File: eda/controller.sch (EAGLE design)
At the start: 17 parts, among them U1 STM32F405/7R, Y1 8 MHz/C_L=15 pF

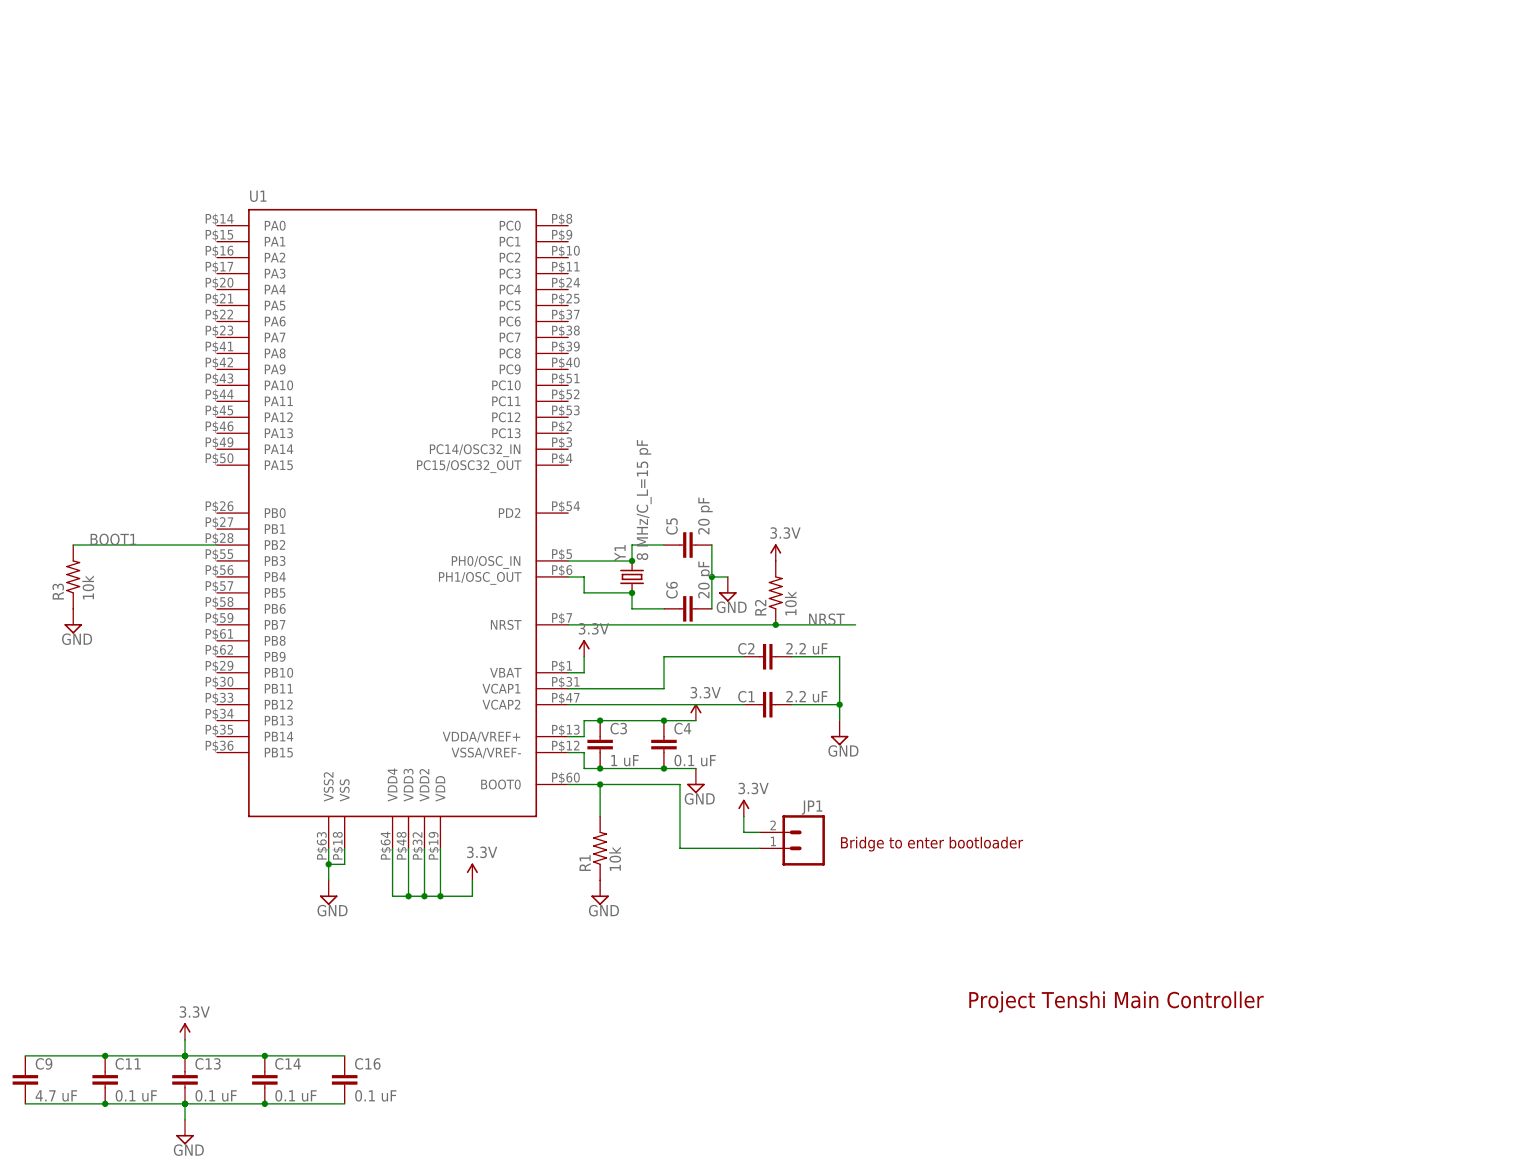
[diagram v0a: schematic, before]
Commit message: Added microSD, LEDs, and pushbuttons
Change-Id: If977962832517d88606b7228ccc3fdc4a6470d0a
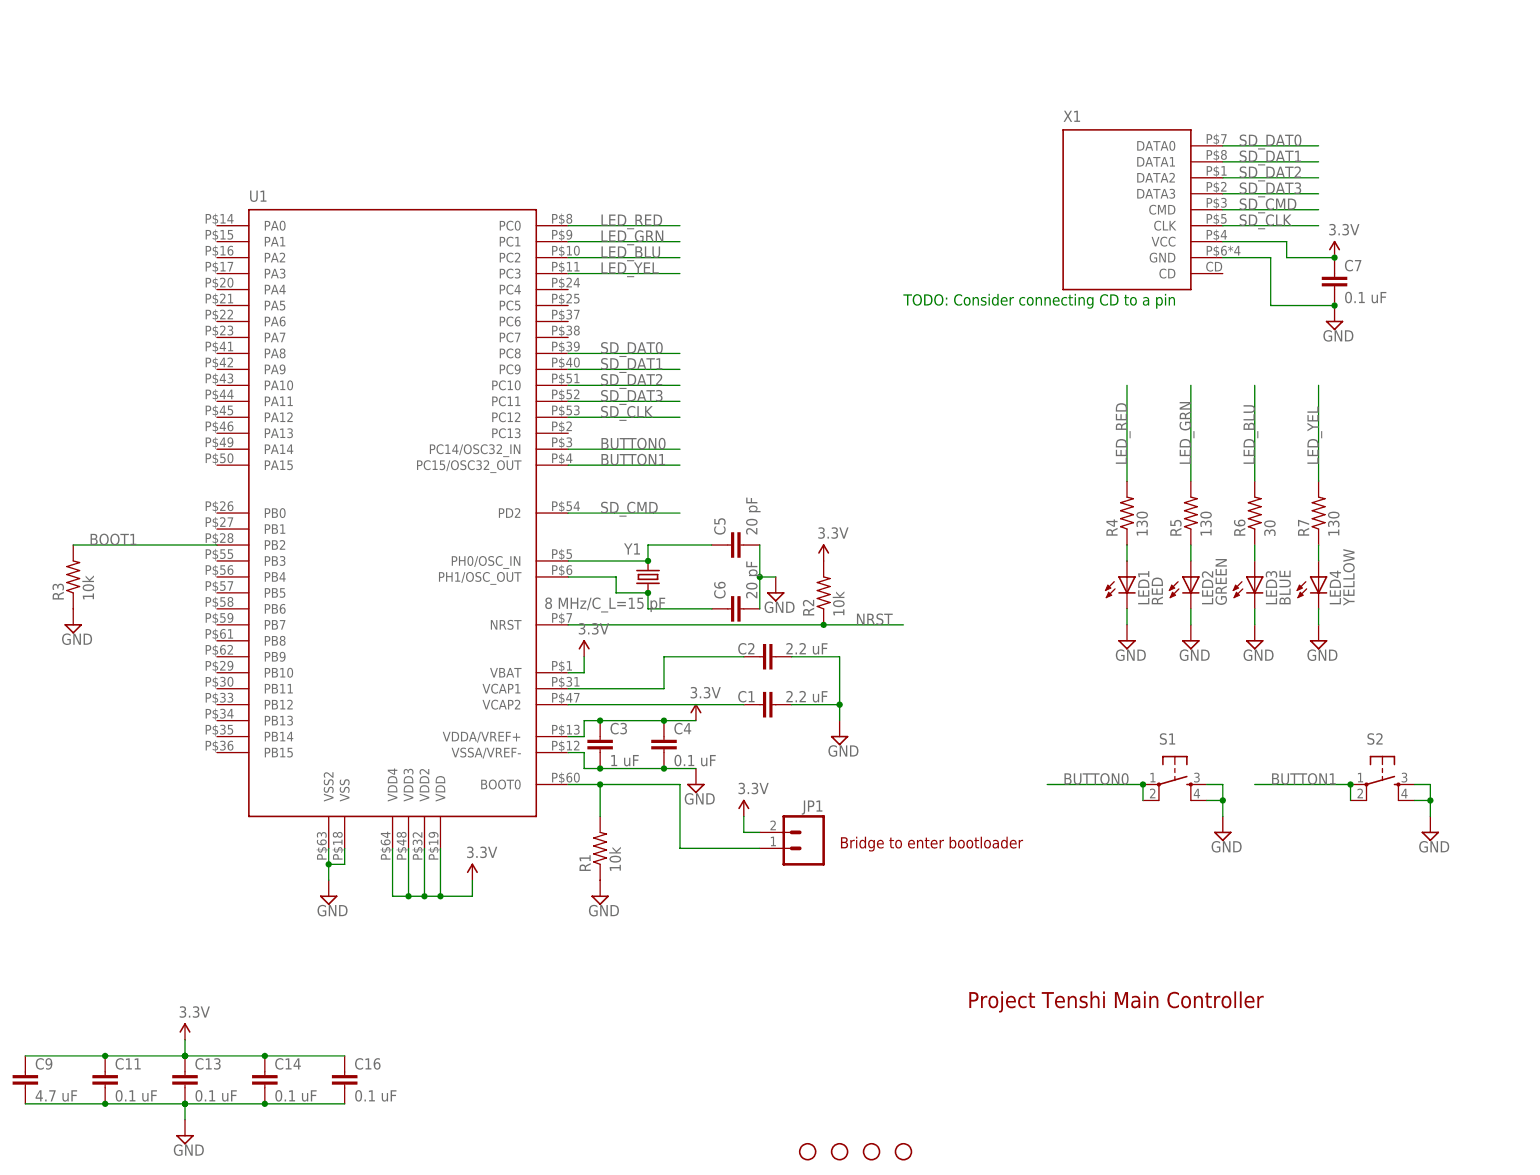
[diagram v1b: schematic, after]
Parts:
- added C7: 0.1 uF, pie:CAP0603-CAP
- added LED1: RED, pie:LED0805
- added LED2: GREEN, pie:LED0805
- added LED3: BLUE, pie:LED0805
- added LED4: YELLOW, pie:LED0805
- added R4, R5, R7: 130, pie:R-US_R0603
- added R6: 30, pie:R-US_R0603
- added S1, S2: (no value), pie:TAC_SWITCHPTH
- added STANDOFF1, STANDOFF2, STANDOFF3, STANDOFF4: STAND-OFF, pie:STAND-OFF
- added X1: MICROSD-SOCKETAMPHENOL, pie:MICROSD-SOCKETAMPHENOL
- C9: device pie:CAP0603-CAP -> pie:CAP0805
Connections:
- new net BUTTON0: S1.1, S1.2, U1.PC14/OSC32_IN
- new net BUTTON1: S2.1, S2.2, U1.PC15/OSC32_OUT
- new net LED_BLU: R6.2, U1.PC2
- new net LED_GRN: R5.2, U1.PC1
- new net LED_RED: R4.2, U1.PC0
- new net LED_YEL: R7.2, U1.PC3
- new net N$5: LED1.A, R4.1
- new net N$7: LED2.A, R5.1
- new net N$8: LED3.A, R6.1
- new net N$9: LED4.A, R7.1
- new net SD_CLK: U1.PC12, X1.CLK
- new net SD_CMD: U1.PD2, X1.CMD
- new net SD_DAT0: U1.PC8, X1.DATA0
- new net SD_DAT1: U1.PC9, X1.DATA1
- new net SD_DAT2: U1.PC10, X1.DATA2
- new net SD_DAT3: U1.PC11, X1.DATA3
- net 3.3V: now also C7.1, X1.VCC
- net GND: now also C7.2, LED1.C, LED2.C, LED3.C, LED4.C, S1.3, S1.4, S2.3, S2.4, X1.GND
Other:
- note added: "TODO: Consider connecting CD to a pin"
- moved on the sheet: C5, C6, R2, Y1

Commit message: Add RS-485 transceivers
Change-Id: Ic10afedf46a3cd01506eb7da054e21ef5b864761
Reviewed-on: https://robertou.com/gerrit/185
Tested-by: Jenkins CI
Reviewed-by: Kyle Zentner <kylezentner@pioneers.berkeley.edu>
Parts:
- added C10, C12, C15, C8: 0.1 uF, pie:CAP0603-CAP
- added JP2: (no value), pie:M031X03-MTA
- added R10, R11, R8, R9: 10k, pie:R-US_R0603
- added U$13, U$14, U$15, U$16: SENSOR_CONPTH, pie:SENSOR_CONPTH
- added U2, U3, U4, U5: ISL83491SOIC, pie:ISL83491SOIC
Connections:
- new net 5V: C10.1, C12.1, C15.1, C8.1, U$13.1, U$13.8, U$14.1, U$14.8, U$15.1, U$15.8, U$16.1, U$16.8, U2.VCC, U3.VCC, U4.VCC, U5.VCC
- new net A_TX1_N: U$13.5, U2.Z
- new net A_TX1_P: U$13.3, U2.Y
- new net A_TX2_N: U$14.5, U3.Z
- new net A_TX2_P: U$14.3, U3.Y
- new net A_TX3_N: U$15.5, U4.Z
- new net A_TX3_P: U$15.3, U4.Y
- new net A_TX4_N: U$16.5, U5.Z
- new net A_TX4_P: U$16.3, U5.Y
- new net B_RX1_N: U$13.4, U2.B
- new net B_RX1_P: U$13.6, U2.A
- new net B_RX2_N: U$14.4, U3.B
- new net B_RX2_P: U$14.6, U3.A
- new net B_RX3_N: U$15.4, U4.B
- new net B_RX3_P: U$15.6, U4.A
- new net B_RX4_N: U$16.4, U5.B
- new net B_RX4_P: U$16.6, U5.A
- new net FLAG_BLU: JP2.2, U1.PB5
- new net FLAG_YEL: JP2.3, U1.PB4
- new net RS485_1_RX: U1.PA1, U2.RO
- new net RS485_1_TX: U1.PA0, U2.DI
- new net RS485_1_TXEN: R8.2, U1.PB3, U2.DE
- new net RS485_2_RX: U1.PA3, U3.RO
- new net RS485_2_TX: U1.PA2, U3.DI
- new net RS485_2_TXEN: R9.2, U1.PC4, U3.DE
- new net RS485_3_RX: U1.PB7, U4.RO
- new net RS485_3_TX: U1.PB6, U4.DI
- new net RS485_3_TXEN: R10.2, U1.PC5, U4.DE
- new net RS485_4_RX: U1.PC7, U5.RO
- new net RS485_4_TX: U1.PC6, U5.DI
- new net RS485_4_TXEN: R11.2, U1.PC13, U5.DE
- net GND: now also C10.2, C12.2, C15.2, C8.2, JP2.1, R10.1, R11.1, R8.1, R9.1, U$13.2, U$13.7, U$14.2, U$14.7, U$15.2, U$15.7, U$16.2, U$16.7, U2.!RE, U2.GND, U3.!RE, U3.GND, U4.!RE, U4.GND, U5.!RE, U5.GND
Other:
- note added: "Microcontroller and misc."
- note added: "RS-485"

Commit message: Added USB and debug connector
Change-Id: Ib7d5965fb4fc0308d7bee20dc58c73a15ffe7a33
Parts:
- added C17: 4.7 uF, pie:CAP0603-CAP
- added C18: 0.01 uF, pie:CAP0603-CAP
- added C19: 0.1 uF, pie:CAP0603-CAP
- added R12: 10k, pie:R-US_R0603
- added U$20: TC2070, pie:TC2070
- added U6: LM3525, pie:LM3525
- added USB1: USB-OTGMICRO-AB, pie:USB-OTGMICRO-AB
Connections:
- new net SWCLK: U$20.13, U1.PA14
- new net SWDIO: U$20.11, U1.PA13
- new net USB_D_N: U1.PA11, USB1.D-
- new net USB_D_P: U1.PA12, USB1.D+
- new net USB_ID: U1.PA10, USB1.ID
- new net USB_OVP: R12.1, U1.PA15, U6.FLAG
- new net USB_VBUS: C17.1, C18.1, U1.PA9, U6.OUT, USB1.VBUS
- new net USB_VBUSEN: U1.PA8, U6.EN
- net 3.3V: now also R12.2, U$20.1
- net 5V: now also C19.1, U6.IN
- net GND: now also C17.2, C18.2, C19.2, U$20.12, U$20.14, U6.GND, USB1.GND
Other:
- note added: "USB, SWD"

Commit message: Added radios
Option to populate one of either an XBee or a HM-10 CC2540 BTLE module

Change-Id: Icec511c4544f83c87418f72e5724f6f69ffe172d
Reviewed-on: https://robertou.com/gerrit/187
Tested-by: Jenkins CI
Reviewed-by: Kyle Zentner <kylezentner@pioneers.berkeley.edu>
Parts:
- added C20: 4.7 uF, pie:CAP0805
- added C21: 0.1 uF, pie:CAP0603-CAP
- added LED5: RED, pie:LED0805
- added R13: 130, pie:R-US_R0603
- added U$22: BLE-HM-10, pie:BLE-HM-10
- added U$23: XBEE-1B2, pie:XBEE-1B2
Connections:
- new net BTLE_DEBUG_C: U$20.4, U$22.P2.1
- new net BTLE_DEBUG_D: U$20.3, U$22.P2.2
- new net N$10: LED5.A, R13.1
- new net RADIO_CLK: U$22.P1.5/UART_RTS, U1.PB12
- new net RADIO_LED: R13.2, U$22.P1.2, U$23.RSSI
- new net RADIO_RX_MISO: U$22.P1.7/UART_RX, U$23.DOUT, U1.PB11
- new net RADIO_TX_MOSI: U$22.P1.6/UART_TX, U$23.DIN, U1.PB10
- net 3.3V: now also C20.1, C21.1, U$22.3.3V, U$23.VDD
- net GND: now also C20.2, C21.2, LED5.C, U$22.GND1, U$22.GND2, U$22.GND3, U$22.GND4, U$23.GND
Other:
- note added: "Populate only one!"
- note added: "Radio"

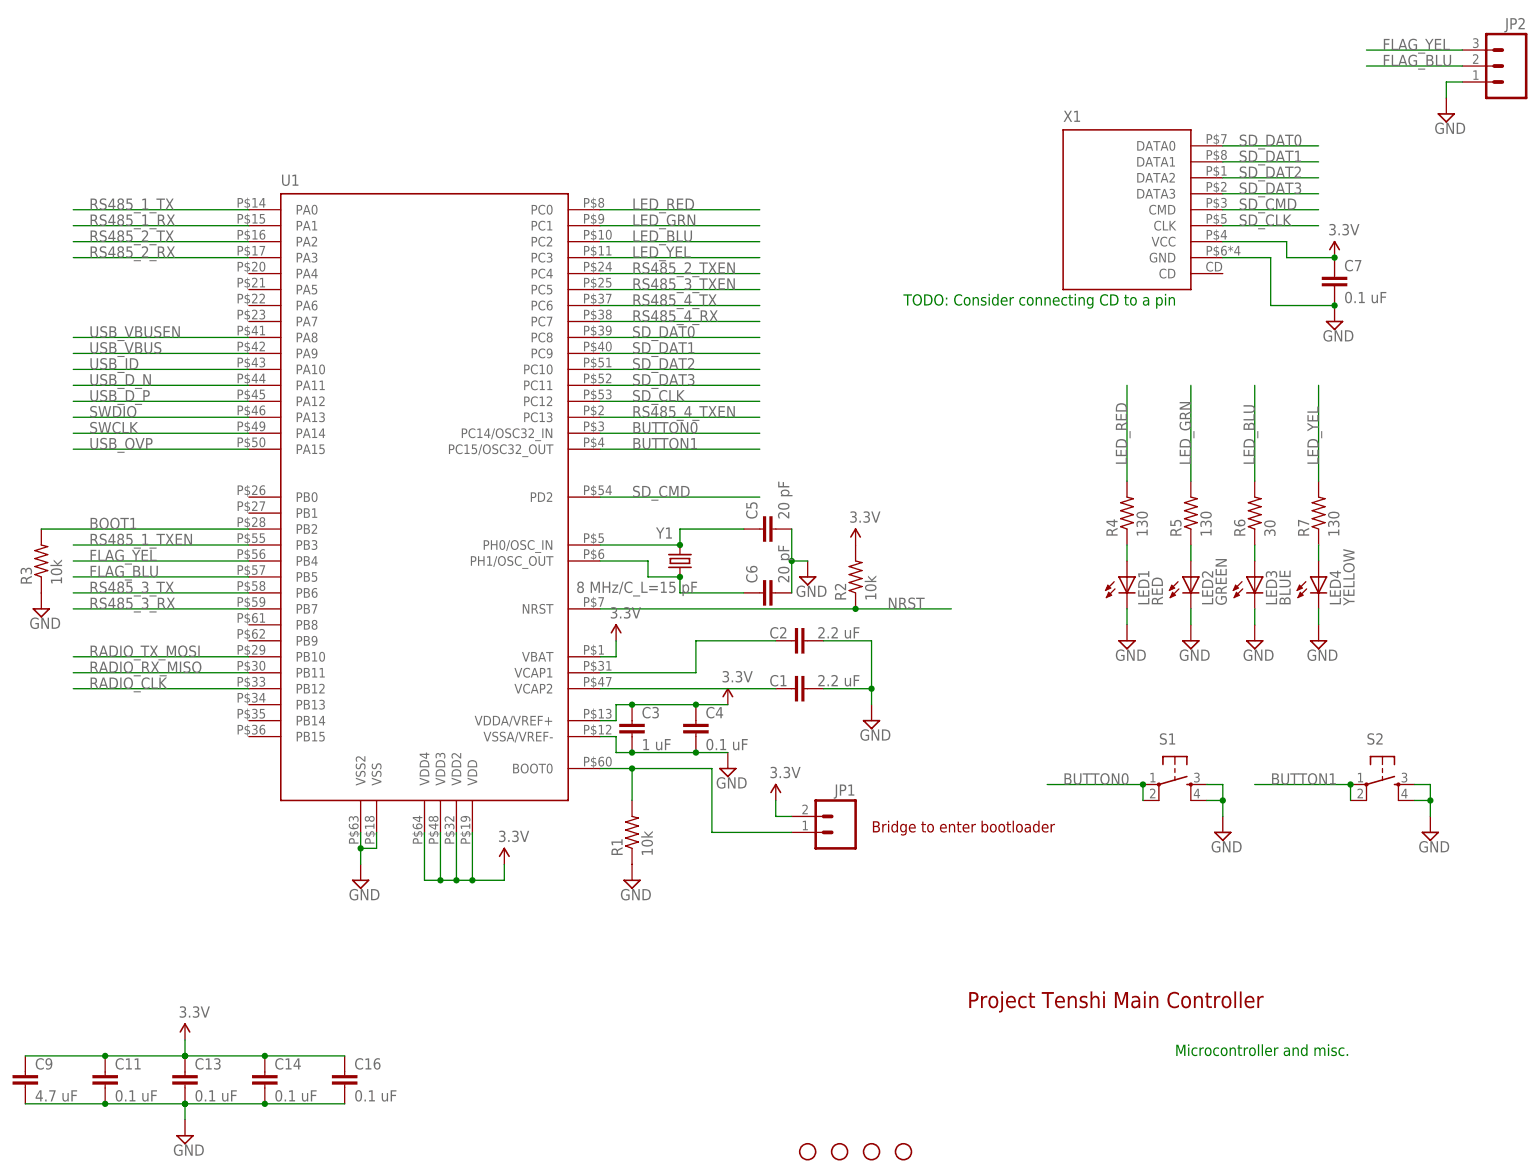
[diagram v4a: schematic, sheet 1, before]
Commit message: Added "legacy" I2C/SPI connectors
Change-Id: Ib85421b65eac117357e296d94d9723e6ac840520
Reviewed-on: https://robertou.com/gerrit/188
Tested-by: Jenkins CI
Reviewed-by: Kyle Zentner <kylezentner@pioneers.berkeley.edu>
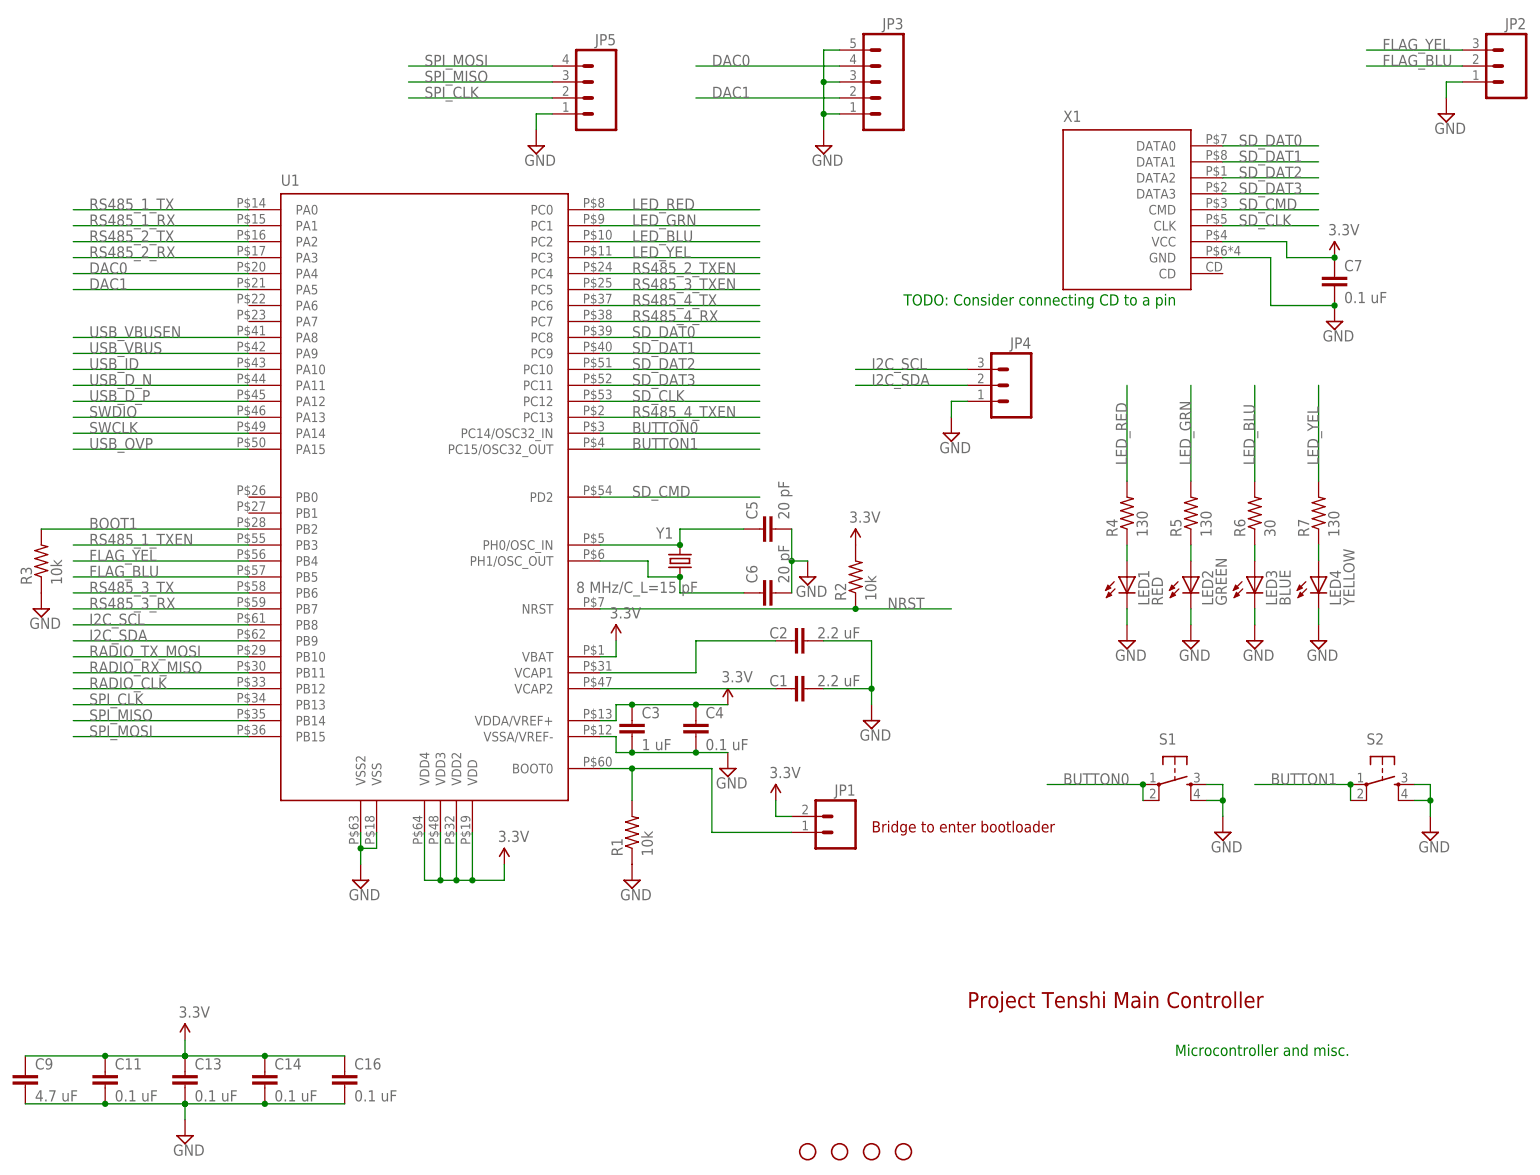
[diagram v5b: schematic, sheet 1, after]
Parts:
- added JP3: (no value), pie:M05MTA
- added JP4: (no value), pie:M031X03-MTA
- added JP5: (no value), pie:M041X04-MTA
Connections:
- new net DAC0: JP3.4, U1.PA4
- new net DAC1: JP3.2, U1.PA5
- new net I2C_SCL: JP4.3, U1.PB8
- new net I2C_SDA: JP4.2, U1.PB9
- new net SPI_CLK: JP5.2, U1.PB13
- new net SPI_MISO: JP5.3, U1.PB14
- new net SPI_MOSI: JP5.4, U1.PB15
- net GND: now also JP3.1, JP3.3, JP3.5, JP4.1, JP5.1
